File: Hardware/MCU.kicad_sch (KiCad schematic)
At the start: 33 parts, among them SW1 reset, SW2 MCU_BOOT, U7 STM32H743VITx, Y1 ASE-8.000MHZ-LC-T

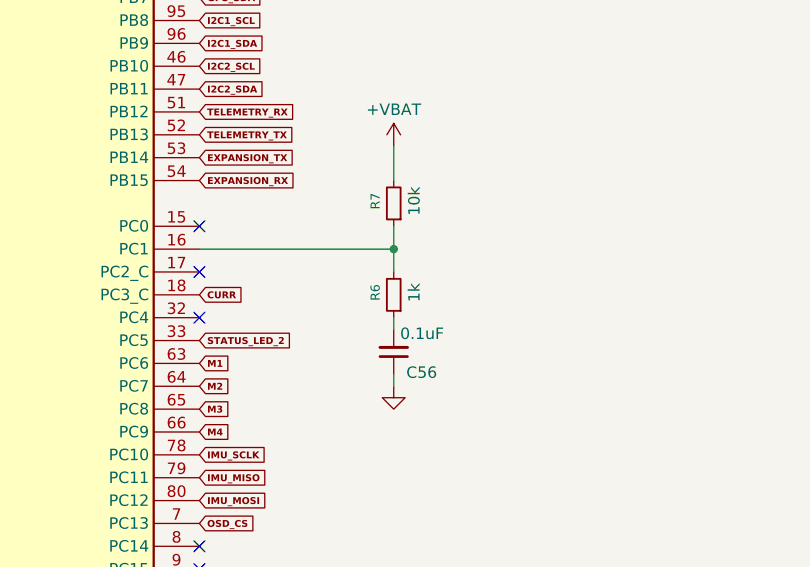
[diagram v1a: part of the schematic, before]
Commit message: corrected vavlues of cap
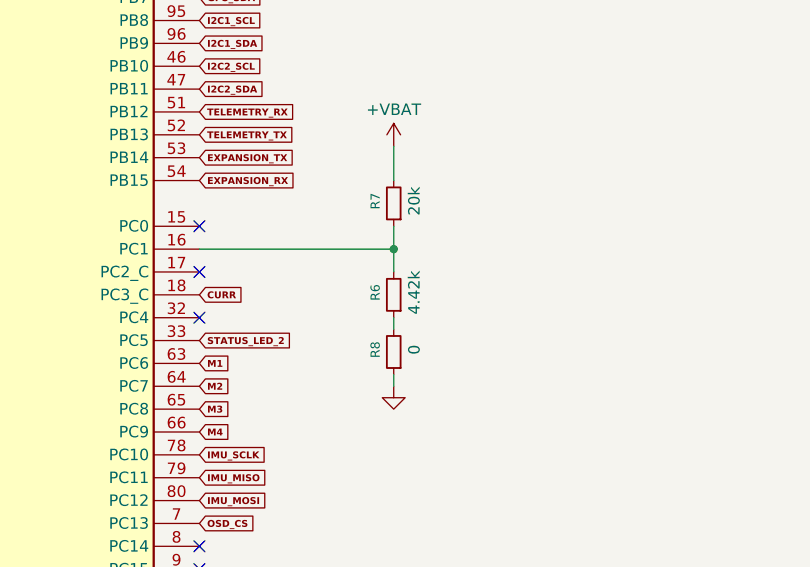
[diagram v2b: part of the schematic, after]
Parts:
- removed C56: 0.1uF, Capacitor_SMD:C_0402_1005Metric, symbol Device:C_Small
- added R8: 0, Resistor_SMD:R_0402_1005Metric, symbol Device:R_Small
- R6: value 1k -> 4.42k
- R7: value 10k -> 20k
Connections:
- net GND: now also R8.1
- net at R6.1: now also R8.2
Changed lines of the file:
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@@
 			)
 		)
-		(property "Value" "10k"
+		(property "Value" "20k"
 			(at 238.506 136.906 90)
 			(show_name no)
@@
 	)
 	(symbol
+		(lib_id "Device:R_Small")
+		(at 236.22 153.67 180)
+		(unit 1)
+		(body_style 1)
+		(exclude_from_sim no)
+		(in_bom yes)
+		(on_board yes)
+		(in_pos_files yes)
+		(dnp no)
+		(property "Reference" "R8"
+			(at 234.188 153.416 90)
+			(show_name no)
+			(do_not_autoplace no)
+			(effects
+				(font
+					(size 1.016 1.016)
+				)
+			)
+		)
+		(property "Value" "0"
+			(at 238.506 153.416 90)
+			(show_name no)
+			(do_not_autoplace no)
+			(effects
+				(font
+					(size 1.27 1.27)
+				)
+			)
+		)
+		(property "Footprint" "Resistor_SMD:R_0402_1005Metric"
+			(at 236.22 153.67 0)
+			(hide yes)
+			(show_name no)
+			(do_not_autoplace no)
+			(effects
+				(font
+					(size 1.27 1.27)
+				)
+			)
+		)
+		(property "Datasheet" ""
+			(at 236.22 153.67 0)
+			(hide yes)
+			(show_name no)
+			(do_not_autoplace no)
+			(effects
+				(font
+					(size 1.27 1.27)
+				)
+			)
+		)
+		(property "Description" "Resistor, small symbol"
+			(at 236.22 153.67 0)
+			(hide yes)
+			(show_name no)
+			(do_not_autoplace no)
+			(effects
+				(font
+					(size 1.27 1.27)
+				)
+			)
+		)
+		(property "Link" ""
+			(at 236.22 153.67 90)
+			(hide yes)
+			(show_name no)
+			(do_not_autoplace no)
+			(effects
+				(font
+					(size 1.27 1.27)
+				)
+			)
+		)
+		(pin "1"
+		)
+		(pin "2"
+		)
+		(instances
+			(project "Flight Controller"
+				(path "/affbaa1c-796a-43e2-b357-d8056264fe45/8463a60f-8f72-494c-88d1-488c894f8e30"
+					(reference "R8")
+					(unit 1)
+				)
+			)
+		)
+	)
+	(symbol
 		(lib_id "power:+3.3V")
 		(at 36.83 45.72 0)
@@
 			)
 		)
-		(property "Value" "1k"
+		(property "Value" "4.42k"
 			(at 238.506 147.066 90)
 			(show_name no)
@@
 					(unit 1)
 				)
-			)
-		)
-	)
-	(symbol
-		(lib_id "Device:C_Small")
-		(at 236.22 153.67 180)
-		(unit 1)
-		(body_style 1)
-		(exclude_from_sim no)
-		(in_bom yes)
-		(on_board yes)
-		(in_pos_files yes)
-		(dnp no)
-		(property "Reference" "C56"
-			(at 241.046 155.956 0)
-			(show_name no)
-			(do_not_autoplace no)
-			(effects
-				(font
-					(size 1.27 1.27)
-				)
-				(justify left)
-			)
-		)
-		(property "Value" "0.1uF"
-			(at 241.808 151.638 0)
-			(show_name no)
-			(do_not_autoplace no)
-			(effects
-				(font
-					(size 1.27 1.27)
-				)
-				(justify left)
-			)
-		)
-		(property "Footprint" "Capacitor_SMD:C_0402_1005Metric"
-			(at 236.22 153.67 0)
-			(hide yes)
-			(show_name no)
-			(do_not_autoplace no)
-			(effects
-				(font
-					(size 1.27 1.27)
-				)
-			)
-		)
-		(property "Datasheet" ""
-			(at 236.22 153.67 0)
-			(hide yes)
-			(show_name no)
-			(do_not_autoplace no)
-			(effects
-				(font
-					(size 1.27 1.27)
-				)
-			)
-		)
-		(property "Description" "Unpolarized capacitor, small symbol"
-			(at 236.22 153.67 0)
-			(hide yes)
-			(show_name no)
-			(do_not_autoplace no)
-			(effects
-				(font
-					(size 1.27 1.27)
-				)
-			)
-		)
-		(property "Link" ""
-			(at 236.22 153.67 0)
-			(hide yes)
-			(show_name no)
-			(do_not_autoplace no)
-			(effects
-				(font
-					(size 1.27 1.27)
-				)
-			)
-		)
-		(pin "1"
-		)
-		(pin "2"
-		)
-		(instances
-			(project "Flight Controller"
-				(path "/affbaa1c-796a-43e2-b357-d8056264fe45/8463a60f-8f72-494c-88d1-488c894f8e30"
-					(reference "C56")
-					(unit 1)
-				)
